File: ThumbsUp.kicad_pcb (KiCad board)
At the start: 2 copper layers, 247.3 x 280.2 mm, 154 parts, among them IC1 RP2040, IC2 W25Q128JVSIM, IC3 RP2040, IC4 W25Q128JVSIM, J1 Conn_01x04_Male, J10 Raiser_Male, J11 Raiser_Female, J12 Raiser_Male, J13 Raiser_Female, J14 Raiser_Male, J15 Raiser_Female, J16 Raiser_Male, J17 Raiser_Female, J18 Raiser_Male, J19 Raiser_Female, J2 Conn_01x04_Male, J20 Conn_01x04_Female, J21 Conn_01x04_Female, J22 Conn_01x04_Female, J23 Conn_01x04_Female, J24 Conn_01x04_Male, J25 Conn_01x04_Male, J26 Conn_01x04_Male, J27 Conn_01x04_Male, J28 Conn_01x04_Female, J29 Conn_01x04_Female, J3 Conn_01x04_Female, J30 Conn_01x04_Female, J31 Conn_01x04_Female, J32 USB_C_Receptacle_USB2.0, J33 Raiser_Male, J34 Raiser_Female, J35 Raiser_Male, J36 STX-3501-3N, J37 USB_C_Receptacle_USB2.0, J38 Raiser_Female, J39 Raiser_Male, J4 Conn_01x04_Male, J40 Raiser_Female, J41 Raiser_Male, J42 Raiser_Female, J43 Raiser_Male, J44 Raiser_Female, J45 Raiser_Male, J46 STX-3501-3N, J47 Raiser_Female, J48 Raiser_Male, J5 Conn_01x04_Female, J6 Conn_01x04_Male, J7 Conn_01x04_Male, J8 Conn_01x04_Male, J9 Raiser_Female, U1 NCP1117-3.3_SOT223, U2 NCP1117-3.3_SOT223, Y1 ABLS-12.000MHZ-B4-T, Y2 ABLS-12.000MHZ-B4-T

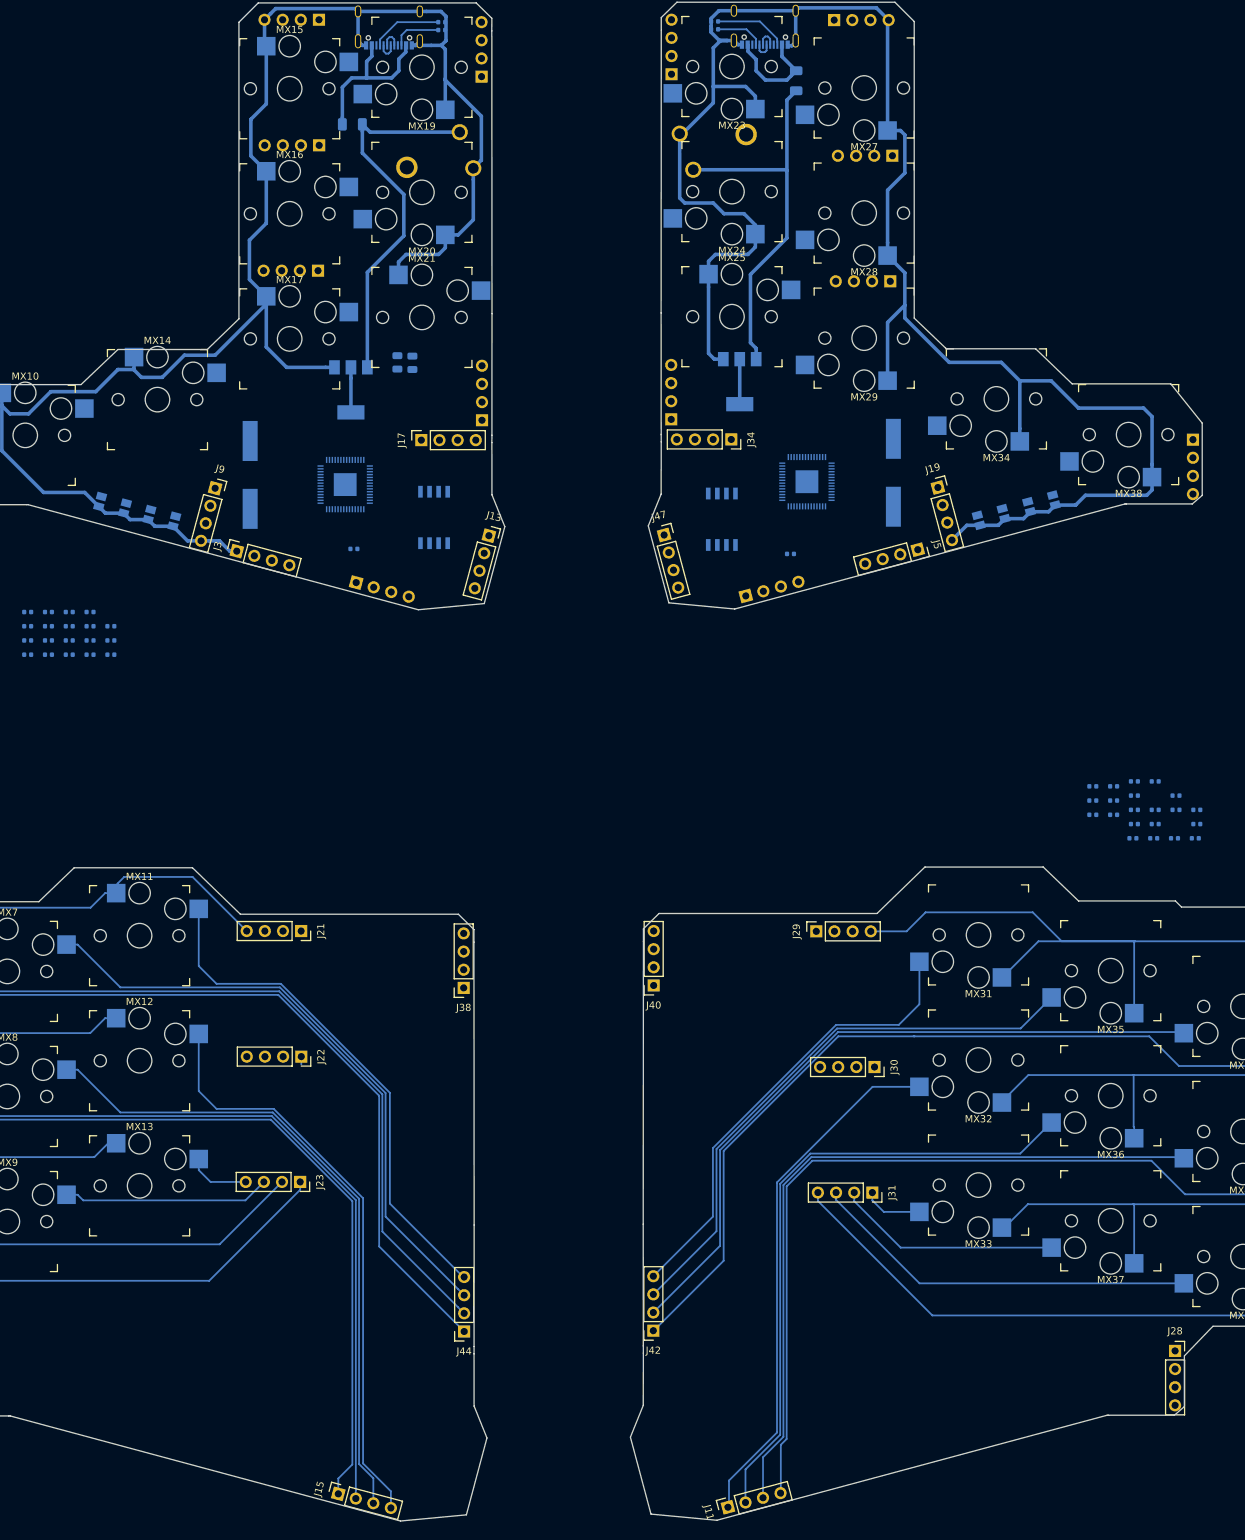
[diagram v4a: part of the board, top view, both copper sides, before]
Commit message: Tracing the plates.
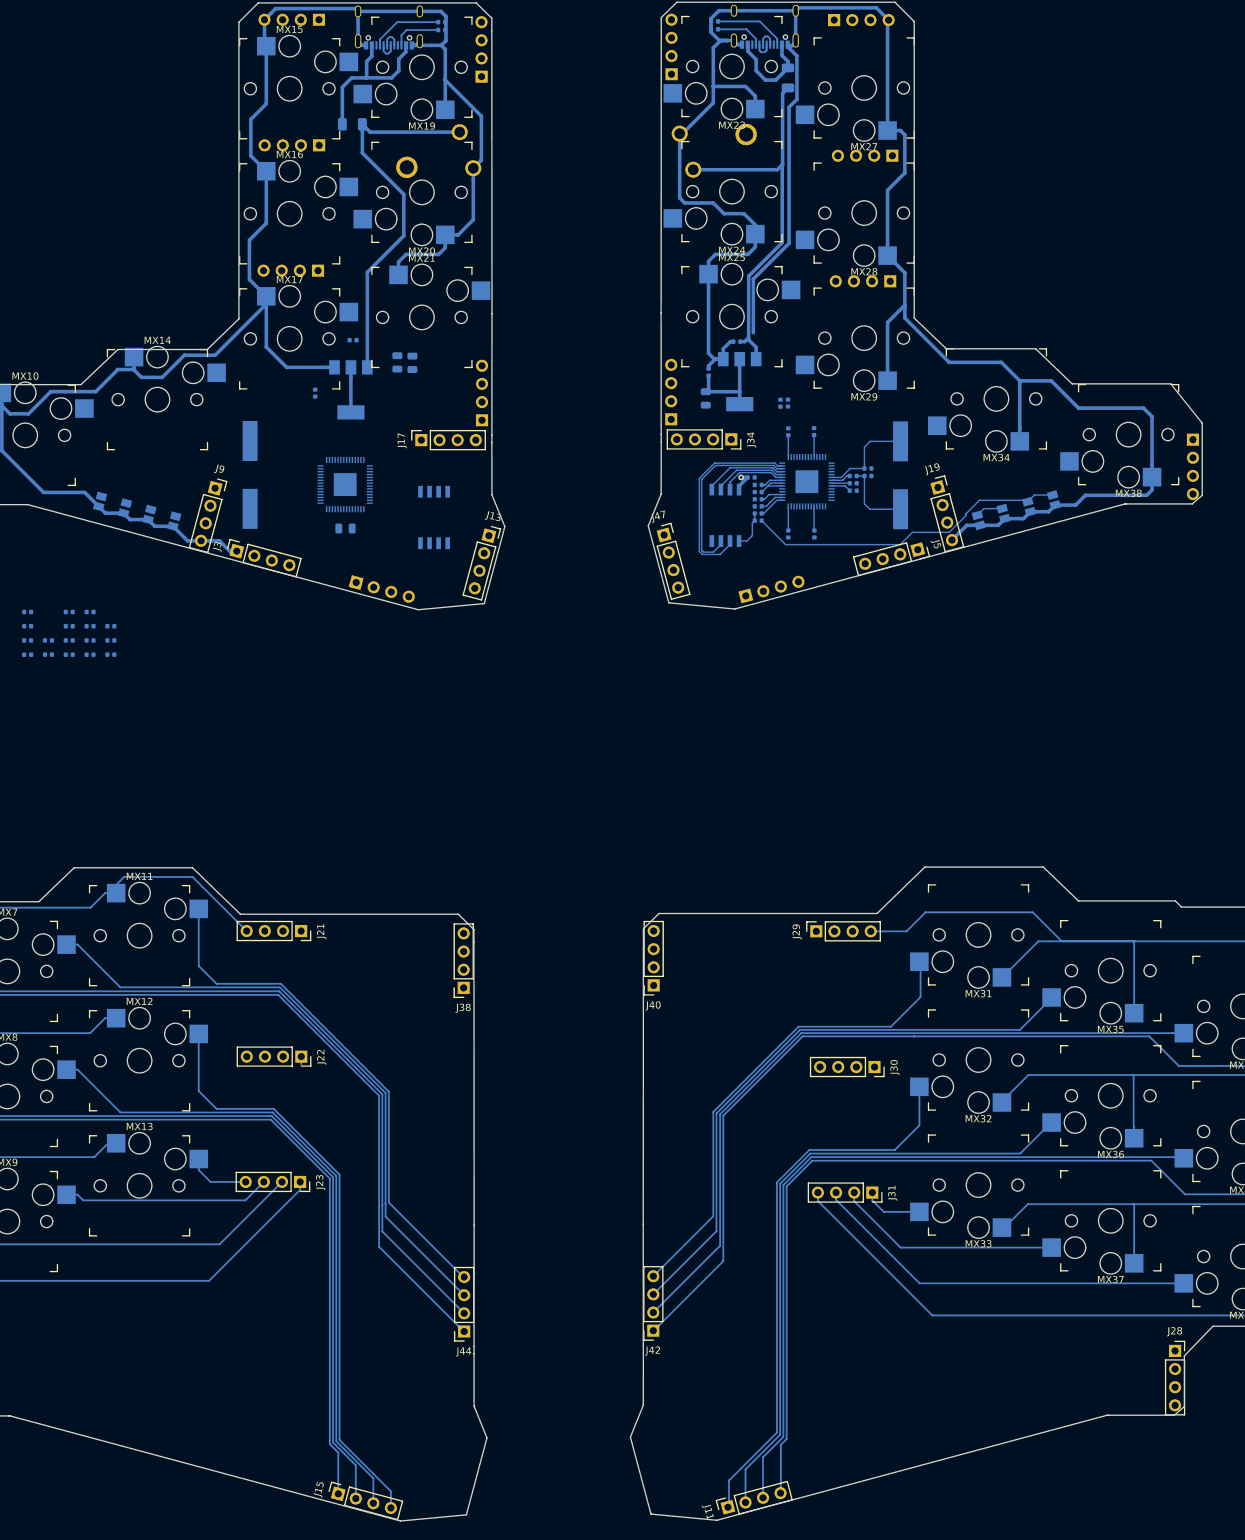
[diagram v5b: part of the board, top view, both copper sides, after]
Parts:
- removed C30: 0.1uF, Capacitor_SMD:C_0402_1005Metric
- R4, R5: value 5.1K -> DNF; footprint Resistor_SMD:R_0402_1005Metric -> Resistor_SMD:R_0805_2012Metric
- moved C18 88.2 mm to (160.7, 441.7), turned to 90 degrees
- moved C8 82.8 mm to (164.6, 437.4), turned to 180 degrees
- moved R14 82.1 mm to (171.8, 446.0), turned to 90 degrees
- moved C27 78.4 mm to (171.8, 450.0), turned to 90 degrees
- moved R15 78.0 mm to (170.7, 446.0), turned to 90 degrees
- moved R12 71.1 mm to (167.6, 462.4), turned to 180 degrees
- moved C26 69.5 mm to (167.6, 457.4), turned to 180 degrees
- moved C24 69.5 mm to (167.6, 459.4), turned to 180 degrees
- moved C31 68.2 mm to (175.4, 464.3), turned to 270 degrees
- moved C20 67.2 mm to (167.6, 458.4), turned to 180 degrees
- moved R16 67.0 mm to (180.9, 456.2)
- moved R13 67.0 mm to (167.6, 461.4)
- moved C32 66.4 mm to (175.4, 450.0), turned to 90 degrees
- moved C19 65.8 mm to (166.6, 456.4)
- moved C22 64.6 mm to (182.9, 456.2)
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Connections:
- IC1 pad 2: TX -> Net-(IC1-Pad2)
- IC3 pad 2: RTX -> Net-(IC3-Pad2)
- IC3 pad 36: Net-(IC3-Pad36) -> K_LWR
- IC3 pad 37: Net-(IC3-Pad37) -> K_RSFT
- IC3 pad 38: Net-(IC3-Pad38) -> K_ENT
- IC3 pad 39: Net-(IC3-Pad39) -> K_SEMICOL
- IC3 pad 40: Net-(IC3-Pad40) -> K_L
- IC3 pad 41: Net-(IC3-Pad41) -> K_K
- R4 pad 1: TX -> L-TIP
- R5 pad 1: RTX -> R-TIP
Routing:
- net L-BASE: track 501.2 -> 549.9 mm
- net Net-(BOOTSEL2-Pad1): track 0.00 -> 45.3 mm
- net +3V3: track 12.6 -> 50.8 mm, vias 0 -> 1
- net RQSPI_SD1: track 0.00 -> 28.4 mm
- net RQSPI_SD2: track 0.00 -> 25.9 mm
- net RXIN: track 0.00 -> 13.5 mm
- net RQSPI_SD0: track 0.00 -> 11.6 mm
- net Net-(C22-Pad1): track 0.00 -> 10.3 mm
- net RQSPI_SCLK: track 0.00 -> 10.2 mm
- net RQSPI_SD3: track 0.00 -> 9.18 mm
- net +1V1: track 0.00 -> 9.12 mm
- net Net-(IC4-Pad1): track 0.00 -> 5.40 mm
- net Net-(RUN2-Pad1): track 0.00 -> 3.86 mm
- net Net-(J11-Pad1): track 73.8 -> 76.9 mm
- net Net-(J42-Pad3): track 79.7 -> 82.7 mm
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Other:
- net class Default: clearance 0.2 -> 0.127; trace_width 0.25 -> 0.2
- net class Power: clearance 0.2 -> 0.127
- rule trace_clearance: 0.2 -> 0.127

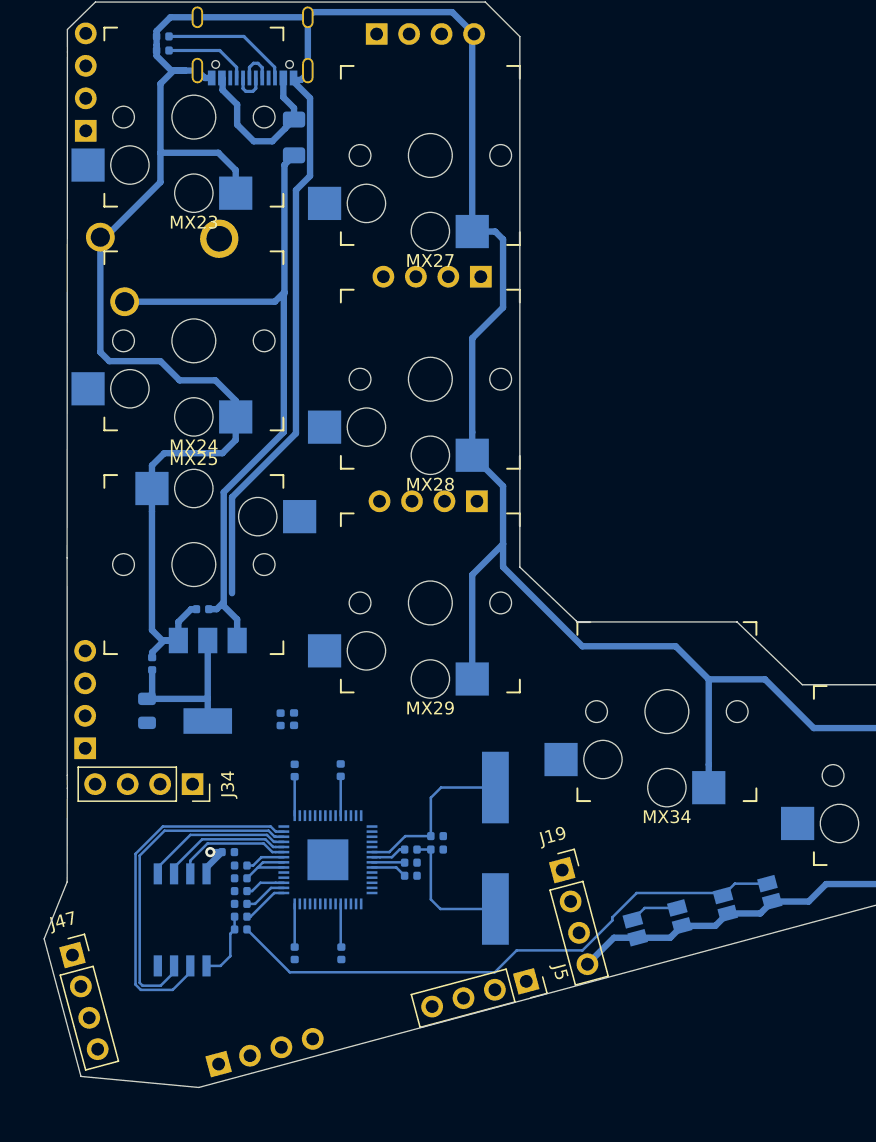
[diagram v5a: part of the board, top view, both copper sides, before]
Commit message: Tracing the plates.
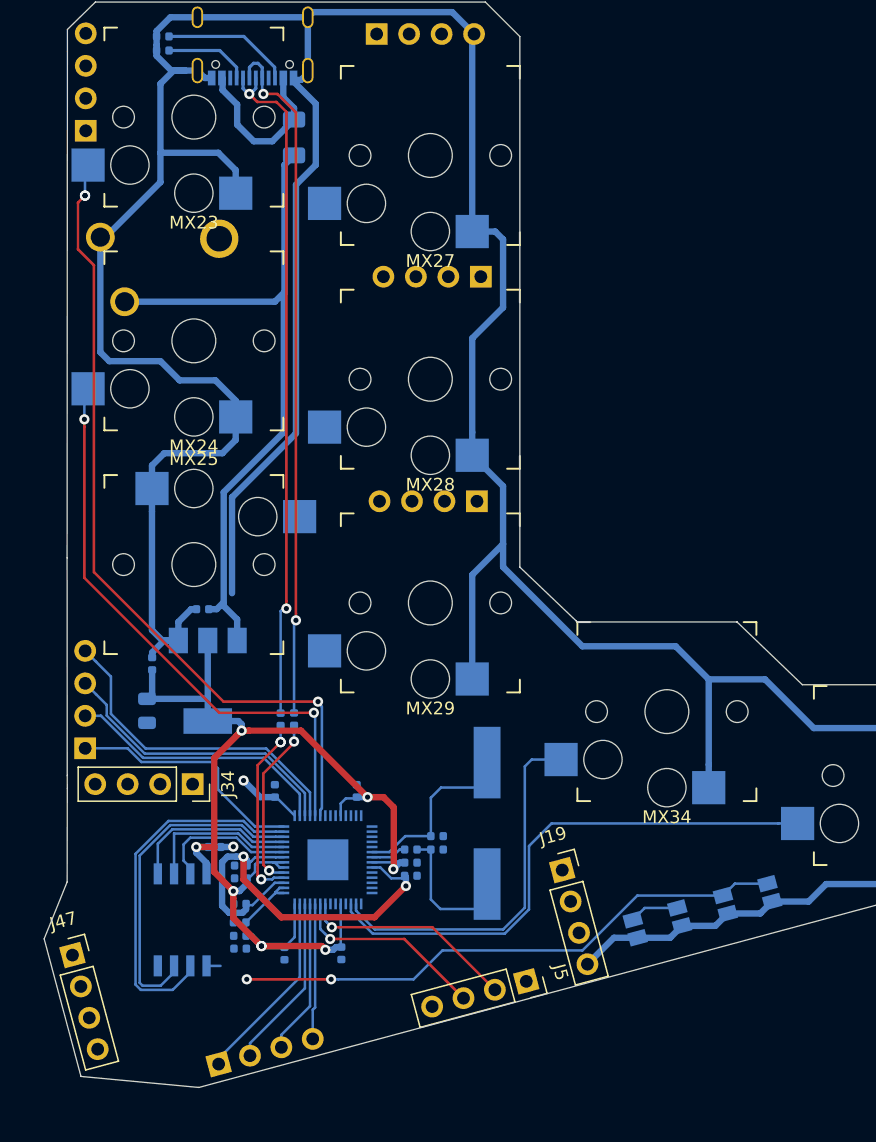
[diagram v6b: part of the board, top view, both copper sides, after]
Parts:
- moved C27 2.23 mm to (170.2, 451.6)
- moved Y2 2.06 mm to (186.8, 454.1)
- moved C32 2.05 mm to (176.7, 451.6)
- moved R13 1.50 mm to (167.5, 462.9)
- moved R12 1.50 mm to (167.5, 463.9)
- moved C25 1.45 mm to (167.5, 461.9)
- moved C19 1.14 mm to (165.5, 456.0)
- moved C24 1.00 mm to (167.5, 460.4)
- moved C23 0.80 mm to (171.0, 464.3)
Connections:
- IC3 pad 11: Net-(IC3-Pad11) -> K_U
- IC3 pad 2: Net-(IC3-Pad2) -> K_P
- IC3 pad 3: Net-(IC3-Pad3) -> K_O
- IC3 pad 30: Net-(IC3-Pad30) -> K_RALT
- IC3 pad 31: Net-(IC3-Pad31) -> K_MNU
- IC3 pad 4: Net-(IC3-Pad4) -> K_I
- IC3 pad 5: Net-(IC3-Pad5) -> K_H
- IC3 pad 56: Net-(IC3-Pad56) -> K_BSPC
- IC3 pad 6: Net-(IC3-Pad6) -> K_Y
- IC3 pad 7: Net-(IC3-Pad7) -> K_N
- IC3 pad 8: Net-(IC3-Pad8) -> K_M
- IC3 pad 9: Net-(IC3-Pad9) -> K_J
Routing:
- net K_Y: track 0.00 -> 63.5 mm, vias 0 -> 3
- net +3V3: track 50.8 -> 108.4 mm, vias 1 -> 9
- net RD+: track 2.92 -> 54.5 mm, vias 0 -> 2
- net RD-: track 2.83 -> 53.9 mm, vias 0 -> 2
- net K_H: track 0.00 -> 45.3 mm, vias 0 -> 2
- net K_MNU: track 0.00 -> 42.7 mm
- net K_RALT: track 0.00 -> 29.2 mm
- net +1V1: track 9.12 -> 36.1 mm, vias 0 -> 2
- net K_I: track 0.00 -> 25.7 mm
- net K_O: track 0.00 -> 23.0 mm
- net K_P: track 0.00 -> 21.0 mm
- net K_BSPC: track 0.00 -> 19.0 mm
- net K_LWR: track 0.00 -> 16.8 mm, vias 0 -> 1
- net K_RSFT: track 0.00 -> 15.4 mm, vias 0 -> 1
- net K_K: track 0.00 -> 15.2 mm
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
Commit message: Somewhat finished the PCB tracing
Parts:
- removed C1: 0.1uF, Capacitor_SMD:C_0402_1005Metric
- added G***: LOGO, Silkscreens:Crowfeet75, B.Cu at (140.7, 575.9)
- added G***: LOGO, Silkscreens:Crowfeet75, F.Cu at (138.9, 564.5)
- added G***: LOGO, Silkscreens:Crowfeet75, F.Cu at (141.2, 407.5)
- R1, R2: footprint Resistor_SMD:R_0805_2012Metric -> Resistor_SMD:R_0402_1005Metric
- moved C4 58.3 mm to (121.2, 460.2)
- moved C5 55.8 mm to (121.2, 461.2)
- moved R5 53.6 mm to (160.2, 445.4), turned to 90 degrees
- moved C2 50.5 mm to (114.6, 468.2), turned to 270 degrees
- moved C13 49.8 mm to (119.2, 463.8)
- moved R4 47.6 mm to (118.5, 468.2), turned to 0 degrees
- moved R6 47.2 mm to (119.2, 461.2)
- moved C16 46.7 mm to (113.8, 456.3), turned to 90 degrees
- moved C15 46.3 mm to (119.2, 462.2)
- moved C6 45.0 mm to (108.7, 456.3), turned to 90 degrees
- moved C12 44.1 mm to (106.5, 465.1), turned to 180 degrees
- moved C3 42.5 mm to (106.4, 462.6), turned to 180 degrees
- moved C7 42.1 mm to (106.4, 466.1), turned to 180 degrees
- moved C14 36.8 mm to (106.4, 461.6), turned to 180 degrees
- moved C17 36.5 mm to (109.4, 468.1), turned to 270 degrees
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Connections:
- IC1 pad 11: Net-(IC1-Pad11) -> K_F
- IC1 pad 12: Net-(IC1-Pad12) -> K_T
- IC1 pad 13: Net-(IC1-Pad13) -> K_G
- IC1 pad 14: Net-(IC1-Pad14) -> K_B
- IC1 pad 15: Net-(IC1-Pad15) -> K_E
- IC1 pad 16: Net-(IC1-Pad16) -> K_W
- IC1 pad 17: Net-(IC1-Pad17) -> K_Q
- IC1 pad 18: Net-(IC1-Pad18) -> K_ESC
- IC1 pad 2: Net-(IC1-Pad2) -> K_WIN
- IC1 pad 26: L-BASE -> Net-(IC1-Pad26)
- IC1 pad 3: Net-(IC1-Pad3) -> K_LALT
- IC1 pad 36: Net-(IC1-Pad36) -> K_D
- IC1 pad 37: Net-(IC1-Pad37) -> K_S
- IC1 pad 38: Net-(IC1-Pad38) -> K_A
- IC1 pad 39: Net-(IC1-Pad39) -> K_TAB
- IC1 pad 40: Net-(IC1-Pad40) -> K_RSE
- IC1 pad 41: Net-(IC1-Pad41) -> K_LSFT
- IC1 pad 8: Net-(IC1-Pad8) -> K_V
- IC1 pad 9: Net-(IC1-Pad9) -> K_R
- IC3 pad 26: L-BASE -> Net-(IC3-Pad26)
- R4 pad 1: L-TIP -> +3V3
- R4 pad 2: +3V3 -> L-TIP
- RUN1 pad 1: Net-(RUN1-Pad1) -> Net-(IC1-Pad26)
- RUN1 pad 2: Net-(RUN1-Pad1) -> Net-(IC1-Pad26)
- RUN2 pad 1: Net-(RUN2-Pad1) -> Net-(IC3-Pad26)
- RUN2 pad 2: Net-(RUN2-Pad1) -> Net-(IC3-Pad26)
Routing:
- net L-BASE: track 551.3 -> 780.8 mm, vias 1 -> 26
- net +3V3: track 108.4 -> 213.6 mm, vias 9 -> 17
- net R-TIP: track 0.00 -> 90.2 mm, vias 0 -> 3
- net K_R: track 0.00 -> 66.1 mm
- net L-TIP: track 0.00 -> 64.5 mm, vias 0 -> 1
- net K_T: track 0.00 -> 61.9 mm
- net Net-(IC1-Pad26): track 0.00 -> 57.3 mm, vias 0 -> 2
- net K_U: track 0.00 -> 55.2 mm
- net D+: track 2.93 -> 56.9 mm, vias 0 -> 2
- net D-: track 2.92 -> 56.7 mm, vias 0 -> 2
- net K_F: track 0.00 -> 46.1 mm
- net K_WIN: track 0.00 -> 44.8 mm
- net K_G: track 0.00 -> 40.4 mm
- net K_J: track 0.00 -> 34.4 mm
- net Net-(IC3-Pad26): track 0.00 -> 33.9 mm, vias 0 -> 4
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- added copper zone on B.Cu, net L-BASE
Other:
- board size 247.3 x 280.2 mm -> 247.3 x 260.9 mm

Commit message: Added a missing line SS-N
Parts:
- removed G*** (x3): LOGO, Silkscreens:Crowfeet75
- moved C31 1.04 mm to (176.5, 464.3)
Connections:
- IC1 pad 56: Net-(IC1-Pad56) -> QSPI_SSN
- IC2 pad 1: Net-(IC2-Pad1) -> QSPI_SSN
- IC3 pad 34: Net-(IC3-Pad34) -> K_BSPC
- IC3 pad 56: K_BSPC -> RQSPI_SSN
- IC4 pad 1: Net-(IC4-Pad1) -> RQSPI_SSN
- R12 pad 2: Net-(IC4-Pad1) -> RQSPI_SSN
- R13 pad 1: Net-(IC4-Pad1) -> RQSPI_SSN
- R3 pad 2: Net-(IC2-Pad1) -> QSPI_SSN
- R7 pad 1: Net-(IC2-Pad1) -> QSPI_SSN
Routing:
- net QSPI_SSN: track 0.00 -> 37.5 mm
- net RQSPI_SSN: track 0.00 -> 35.5 mm
- net K_BSPC: track 19.0 -> 44.5 mm, vias 0 -> 2
- net Net-(IC2-Pad1): track 22.2 -> 0.00 mm
- net Net-(IC4-Pad1): track 4.30 -> 0.00 mm
- net K_LALT: track 31.1 -> 27.3 mm
- net K_WIN: track 44.8 -> 43.3 mm
- net +3V3: track 213.6 -> 215.0 mm
